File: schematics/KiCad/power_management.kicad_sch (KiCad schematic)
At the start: 24 parts, among them J3 USB_C, Q1 DMG6601LVT-7, U4 AP2112K-3.3, U5 MP2615AGQ-Z

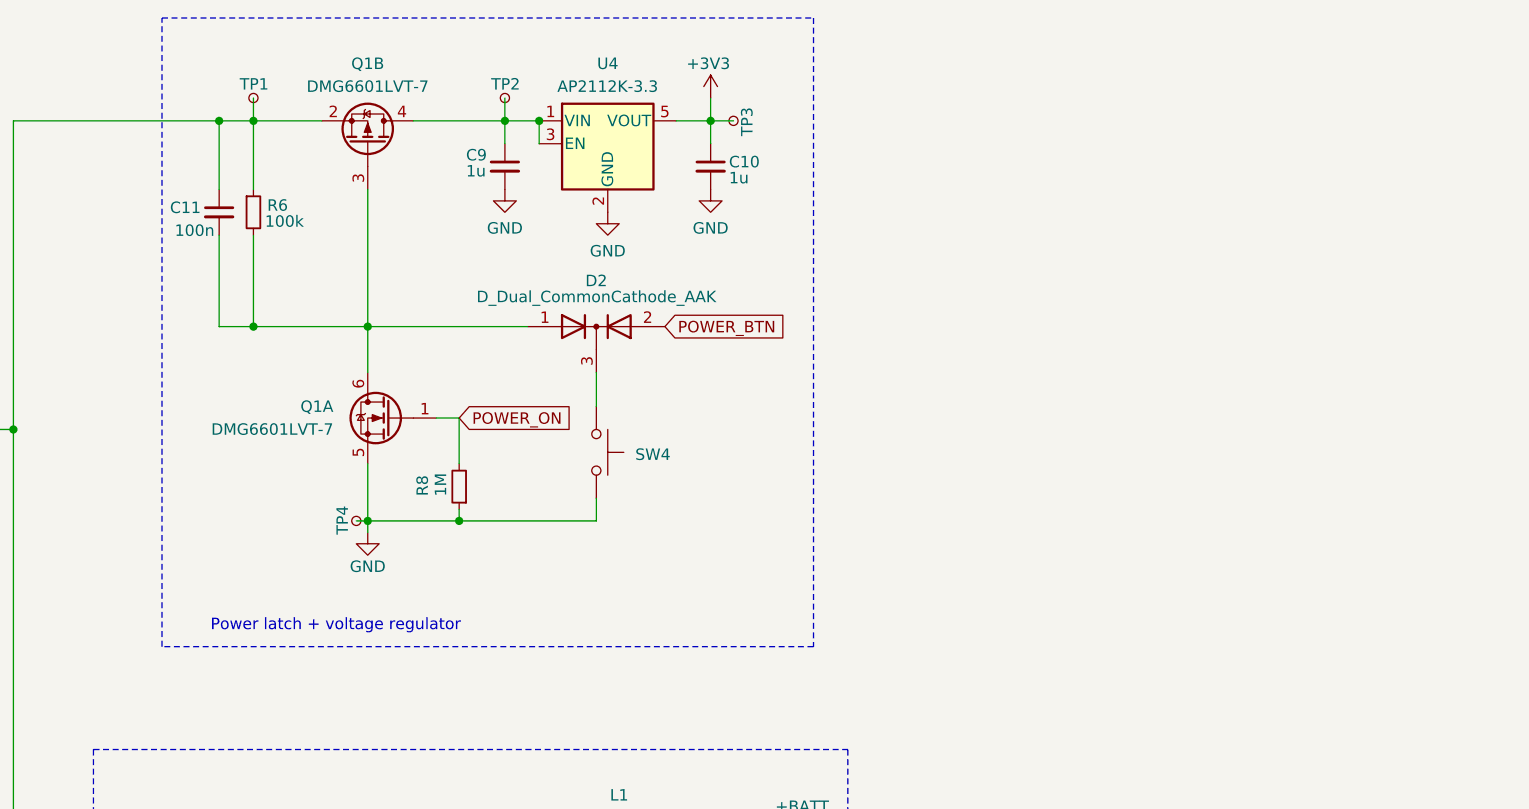
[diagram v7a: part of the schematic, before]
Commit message: add decoupling capacitors
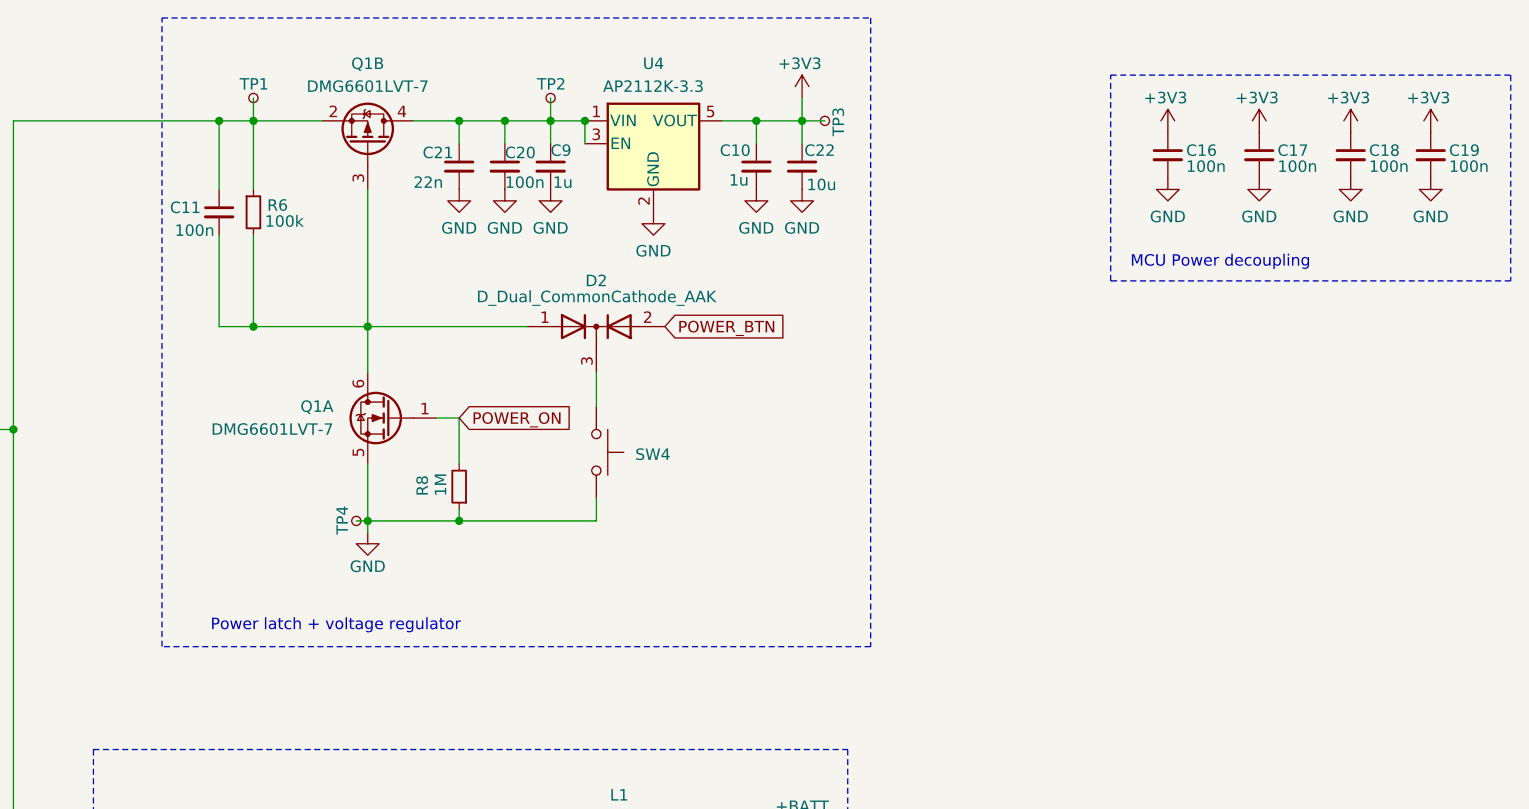
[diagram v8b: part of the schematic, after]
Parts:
- added C16, C17, C18, C19, C20: 100n, Capacitor_SMD:C_0201_0603Metric, symbol Device:C_Small
- added C21: 22n, Capacitor_SMD:C_0201_0603Metric, symbol Device:C_Small
- added C22: 10u, Capacitor_SMD:C_0201_0603Metric, symbol Device:C_Small
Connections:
- net +3V3: now also C16.1, C17.1, C18.1, C19.1, C22.1
- net -BATT: now also C16.2, C17.2, C18.2, C19.2, C20.2, C21.2, C22.2
- net at C9.1, Q1.4 (D), TP2.1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: now also C20.1, C21.1
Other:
- note added: "MCU Power decoupling"
- moved on the sheet: C10, C9, TP2, TP3, U4
